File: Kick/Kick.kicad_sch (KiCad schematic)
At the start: 8 parts, among them J1 CN1 / J11, J2 CN2 / J12, U0 NOIP1SN1300A-QTI, U1 NOIP1SN1300A-QTI, U2 NX3L4053, U3 NX3L4053

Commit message: started PCB routing with new voltage regulators
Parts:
- added C1, C2: C, Capacitor_SMD:C_0603_1608Metric, symbol Device:C
- added U4: MIC5504-1.8YM5, Package_TO_SOT_SMD:SOT-23-5, symbol Regulator_Linear:MIC5504-1.8YM5
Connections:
- net +1V8: now also C2.1, U4.5 (VOUT); no longer J1.5 (Pin_5)
- net +3.3V: now also U4.3 (EN)
- net +3V3: now also C1.1, U4.1 (VIN)
- net GND: now also C1.2, C2.2, U4.2 (GND)
- no-connect marks 101 -> 102

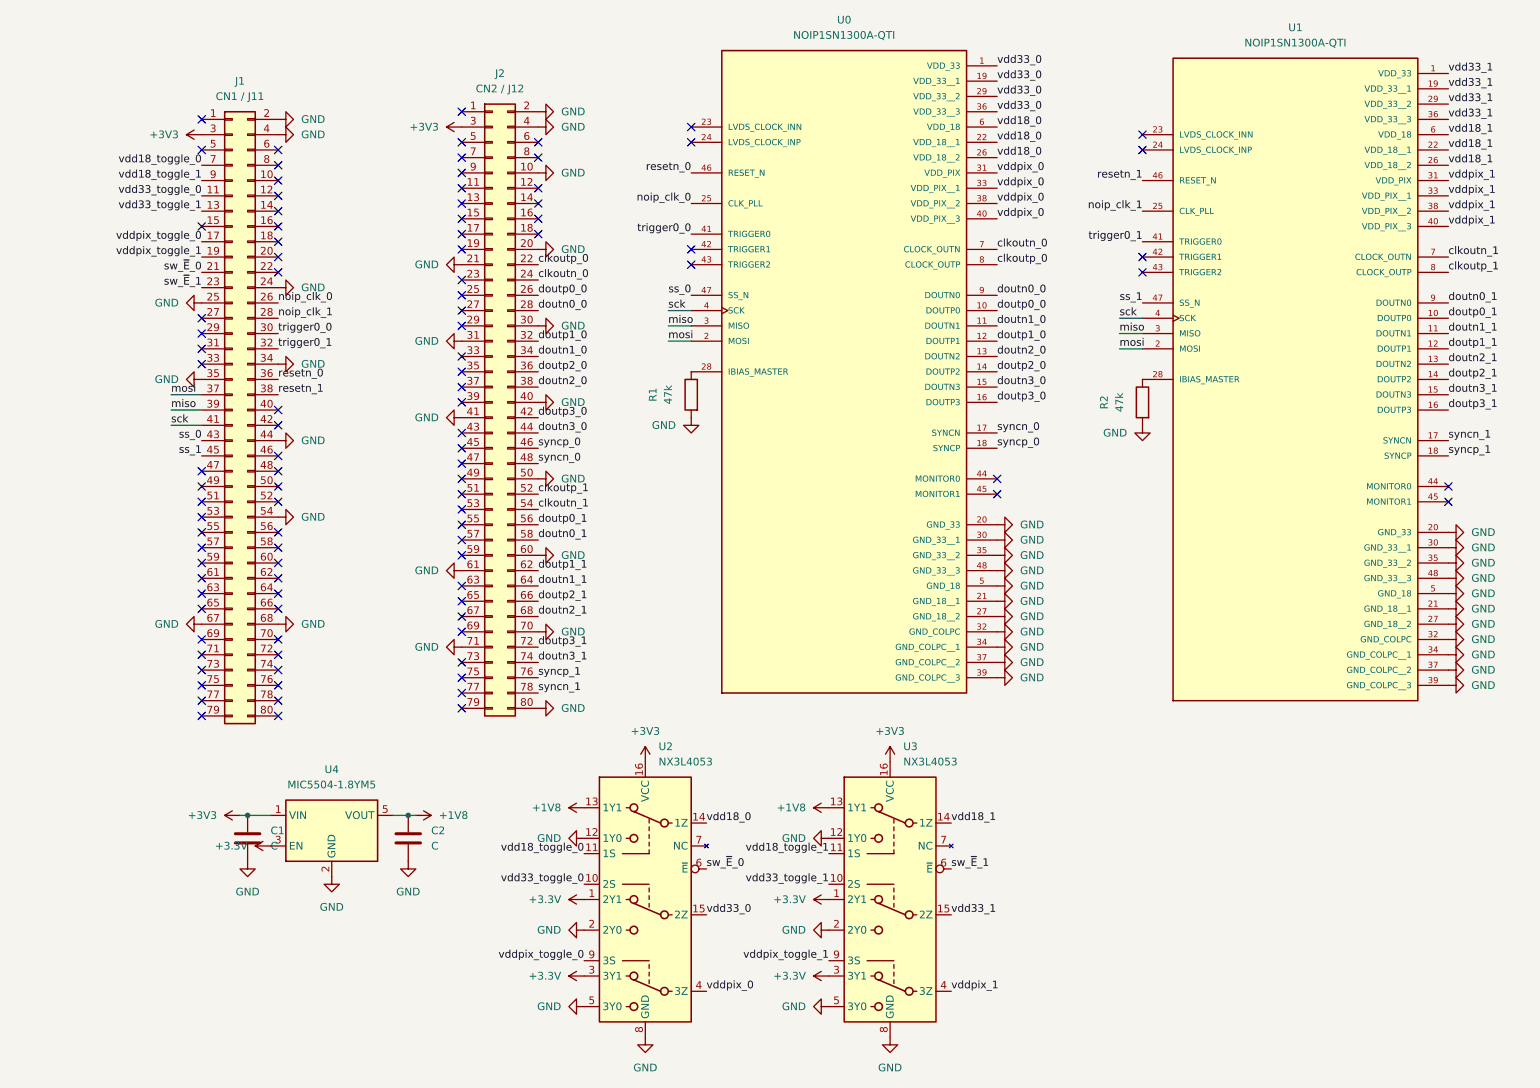
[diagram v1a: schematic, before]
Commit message: acurrate placement of devices, HF impedance calculation
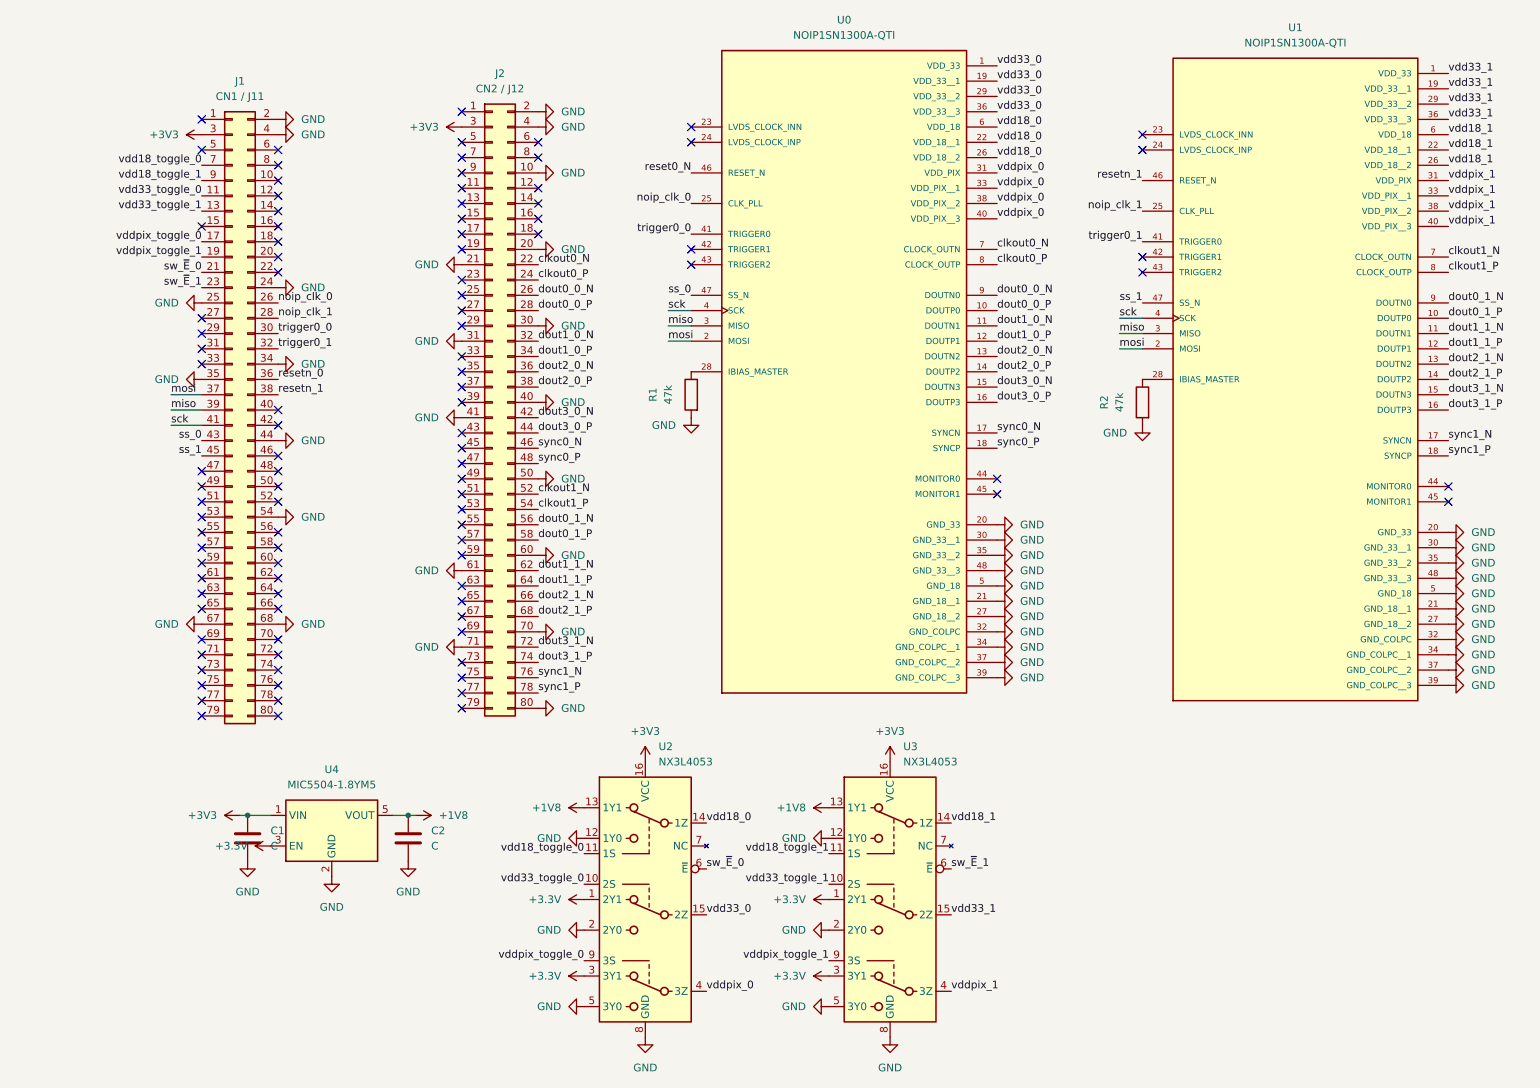
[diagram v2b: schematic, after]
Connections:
- net resetn_0: no longer U0.46 (RESET_N)
- net clkoutn_0 renamed clkout0_N
- net clkout0_N: now also J2.22 (Pin_22); no longer J2.24 (Pin_24)
- net clkoutn_1 renamed clkout1_N
- net clkout1_N: now also J2.52 (Pin_52); no longer J2.54 (Pin_54)
- net clkoutp_0 renamed clkout0_P
- net clkout0_P: now also J2.24 (Pin_24); no longer J2.22 (Pin_22)
- net clkoutp_1 renamed clkout1_P
- net clkout1_P: now also J2.54 (Pin_54); no longer J2.52 (Pin_52)
- net doutn0_0 renamed dout0_0_N
- net dout0_0_N: now also J2.26 (Pin_26); no longer J2.28 (Pin_28)
- net doutn0_1 renamed dout0_1_N
- net dout0_1_N: now also J2.56 (Pin_56); no longer J2.58 (Pin_58)
- net doutn1_0 renamed dout1_0_N
- net dout1_0_N: now also J2.32 (Pin_32); no longer J2.34 (Pin_34)
- net doutn1_1 renamed dout1_1_N
- net dout1_1_N: now also J2.62 (Pin_62); no longer J2.64 (Pin_64)
- net doutn2_0 renamed dout2_0_N
- net dout2_0_N: now also J2.36 (Pin_36); no longer J2.38 (Pin_38)
- net doutn2_1 renamed dout2_1_N
- net dout2_1_N: now also J2.66 (Pin_66); no longer J2.68 (Pin_68)
- net doutn3_0 renamed dout3_0_N
- net dout3_0_N: now also J2.42 (Pin_42); no longer J2.44 (Pin_44)
- net doutn3_1 renamed dout3_1_N
- net dout3_1_N: now also J2.72 (Pin_72); no longer J2.74 (Pin_74)
- net doutp0_0 renamed dout0_0_P
- net dout0_0_P: now also J2.28 (Pin_28); no longer J2.26 (Pin_26)
- net doutp0_1 renamed dout0_1_P
- net dout0_1_P: now also J2.58 (Pin_58); no longer J2.56 (Pin_56)
- net doutp1_0 renamed dout1_0_P
- net dout1_0_P: now also J2.34 (Pin_34); no longer J2.32 (Pin_32)
- net doutp1_1 renamed dout1_1_P
- net dout1_1_P: now also J2.64 (Pin_64); no longer J2.62 (Pin_62)
- net doutp2_0 renamed dout2_0_P
- net dout2_0_P: now also J2.38 (Pin_38); no longer J2.36 (Pin_36)
- net doutp2_1 renamed dout2_1_P
- net dout2_1_P: now also J2.68 (Pin_68); no longer J2.66 (Pin_66)
- net doutp3_0 renamed dout3_0_P
- net dout3_0_P: now also J2.44 (Pin_44); no longer J2.42 (Pin_42)
- net doutp3_1 renamed dout3_1_P
- net dout3_1_P: now also J2.74 (Pin_74); no longer J2.72 (Pin_72)
- net syncn_0 renamed sync0_N
- net sync0_N: now also J2.46 (Pin_46); no longer J2.48 (Pin_48)
- net syncn_1 renamed sync1_N
- net sync1_N: now also J2.76 (Pin_76); no longer J2.78 (Pin_78)
- net syncp_0 renamed sync0_P
- net sync0_P: now also J2.48 (Pin_48); no longer J2.46 (Pin_46)
- net syncp_1 renamed sync1_P
- net sync1_P: now also J2.78 (Pin_78); no longer J2.76 (Pin_76)
- new net reset0_N: U0.46 (RESET_N)
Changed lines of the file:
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@@
 		)
 	)
-	(label "doutp0_1"
-		(at 100.33 105.41 0)
+	(label "dout0_1_P"
+		(at 100.33 107.95 0)
 		(fields_autoplaced yes)
 		(effects
@@
 		)
 	)
-	(label "syncp_0"
-		(at 100.33 92.71 0)
+	(label "sync0_P"
+		(at 100.33 95.25 0)
 		(fields_autoplaced yes)
 		(effects
@@
 		)
 	)
-	(label "syncn_1"
-		(at 100.33 133.35 0)
+	(label "sync1_N"
+		(at 100.33 130.81 0)
 		(fields_autoplaced yes)
 		(effects
@@
 		)
 	)
-	(label "doutn1_1"
+	(label "dout1_1_N"
 		(at 251.46 73.66 0)
 		(fields_autoplaced yes)
@@
 		)
 	)
-	(label "clkoutp_0"
-		(at 100.33 62.23 0)
+	(label "clkout0_P"
+		(at 100.33 64.77 0)
 		(fields_autoplaced yes)
 		(effects
@@
 		)
 	)
-	(label "clkoutn_1"
-		(at 100.33 102.87 0)
+	(label "clkout1_N"
+		(at 100.33 100.33 0)
 		(fields_autoplaced yes)
 		(effects
@@
 		)
 	)
-	(label "doutp1_1"
+	(label "dout1_1_P"
 		(at 251.46 76.2 0)
 		(fields_autoplaced yes)
@@
 		)
 	)
-	(label "doutn2_1"
+	(label "dout2_1_N"
 		(at 251.46 78.74 0)
 		(fields_autoplaced yes)
@@
 		)
 	)
-	(label "syncn_0"
+	(label "sync0_N"
 		(at 176.53 90.17 0)
 		(fields_autoplaced yes)
@@
 		)
 	)
-	(label "doutp1_0"
+	(label "dout1_0_P"
 		(at 176.53 74.93 0)
 		(fields_autoplaced yes)
@@
 		)
 	)
-	(label "doutn0_1"
+	(label "dout0_1_N"
 		(at 251.46 68.58 0)
 		(fields_autoplaced yes)
@@
 		)
 	)
-	(label "syncn_0"
-		(at 100.33 95.25 0)
+	(label "sync0_N"
+		(at 100.33 92.71 0)
 		(fields_autoplaced yes)
 		(effects
@@
 		)
 	)
-	(label "doutp3_1"
-		(at 100.33 125.73 0)
+	(label "dout3_1_P"
+		(at 100.33 128.27 0)
 		(fields_autoplaced yes)
 		(effects
@@
 		)
 	)
-	(label "doutp2_1"
-		(at 100.33 118.11 0)
+	(label "dout2_1_P"
+		(at 100.33 120.65 0)
 		(fields_autoplaced yes)
 		(effects
@@
 		)
 	)
-	(label "doutn3_1"
+	(label "dout3_1_N"
 		(at 251.46 83.82 0)
 		(fields_autoplaced yes)
@@
 		)
 	)
-	(label "doutn0_0"
-		(at 100.33 69.85 0)
+	(label "dout0_0_N"
+		(at 100.33 67.31 0)
 		(fields_autoplaced yes)
 		(effects
@@
 		)
 	)
-	(label "syncn_1"
+	(label "sync1_N"
 		(at 251.46 91.44 0)
 		(fields_autoplaced yes)
@@
 		)
 	)
-	(label "doutp2_1"
+	(label "dout2_1_P"
 		(at 251.46 81.28 0)
 		(fields_autoplaced yes)
@@
 		)
 	)
-	(label "doutn0_1"
-		(at 100.33 107.95 0)
+	(label "dout0_1_N"
+		(at 100.33 105.41 0)
 		(fields_autoplaced yes)
 		(effects
@@
 		)
 	)
-	(label "clkoutp_1"
-		(at 100.33 100.33 0)
+	(label "clkout1_P"
+		(at 100.33 102.87 0)
 		(fields_autoplaced yes)
 		(effects
@@
 		)
 	)
-	(label "doutn1_0"
-		(at 100.33 77.47 0)
+	(label "dout1_0_N"
+		(at 100.33 74.93 0)
 		(fields_autoplaced yes)
 		(effects
@@
 		)
 	)
-	(label "doutp3_0"
-		(at 100.33 87.63 0)
+	(label "dout3_0_P"
+		(at 100.33 90.17 0)
 		(fields_autoplaced yes)
 		(effects
@@
 		)
 	)
-	(label "clkoutn_0"
+	(label "clkout0_N"
 		(at 176.53 59.69 0)
 		(fields_autoplaced yes)
@@
 		)
 	)
-	(label "clkoutp_0"
+	(label "clkout0_P"
 		(at 176.53 62.23 0)
 		(fields_autoplaced yes)
@@
 		)
 	)
-	(label "doutn2_1"
-		(at 100.33 120.65 0)
+	(label "dout2_1_N"
+		(at 100.33 118.11 0)
 		(fields_autoplaced yes)
 		(effects
@@
 		)
 	)
-	(label "doutp0_0"
+	(label "dout0_0_P"
 		(at 176.53 69.85 0)
 		(fields_autoplaced yes)
@@
 		)
 	)
-	(label "doutn3_0"
-		(at 100.33 90.17 0)
+	(label "dout3_0_N"
+		(at 100.33 87.63 0)
 		(fields_autoplaced yes)
 		(effects
@@
 		)
 	)
-	(label "doutn3_0"
+	(label "dout3_0_N"
 		(at 176.53 82.55 0)
 		(fields_autoplaced yes)
@@
 		)
 	)
-	(label "doutp1_0"
-		(at 100.33 74.93 0)
+	(label "dout1_0_P"
+		(at 100.33 77.47 0)
 		(fields_autoplaced yes)
 		(effects
@@
 		)
 	)
-	(label "doutn1_1"
-		(at 100.33 115.57 0)
+	(label "dout1_1_N"
+		(at 100.33 113.03 0)
 		(fields_autoplaced yes)
 		(effects
@@
 		)
 	)
-	(label "syncp_0"
+	(label "sync0_P"
 		(at 176.53 92.71 0)
 		(fields_autoplaced yes)
@@
 		)
 	)
-	(label "doutn3_1"
-		(at 100.33 128.27 0)
+	(label "dout3_1_N"
+		(at 100.33 125.73 0)
 		(fields_autoplaced yes)
 		(effects
@@
 		)
 	)
-	(label "doutp0_0"
-		(at 100.33 67.31 0)
+	(label "dout0_0_P"
+		(at 100.33 69.85 0)
 		(fields_autoplaced yes)
 		(effects
@@
 		)
 	)
-	(label "syncp_1"
-		(at 100.33 130.81 0)
+	(label "sync1_P"
+		(at 100.33 133.35 0)
 		(fields_autoplaced yes)
 		(effects
@@
 		)
 	)
-	(label "doutn1_0"
+	(label "dout1_0_N"
 		(at 176.53 72.39 0)
 		(fields_autoplaced yes)
@@
 		)
 	)
-	(label "doutp3_1"
+	(label "dout3_1_P"
 		(at 251.46 86.36 0)
 		(fields_autoplaced yes)
@@
 		)
 	)
-	(label "syncp_1"
+	(label "sync1_P"
 		(at 251.46 93.98 0)
 		(fields_autoplaced yes)
@@
 		)
 	)
-	(label "doutn2_0"
+	(label "dout2_0_N"
 		(at 176.53 77.47 0)
 		(fields_autoplaced yes)
@@
 		)
 	)
-	(label "doutp2_0"
-		(at 100.33 80.01 0)
+	(label "dout2_0_P"
+		(at 100.33 82.55 0)
 		(fields_autoplaced yes)
 		(effects
@@
 		)
 	)
-	(label "doutp2_0"
+	(label "dout2_0_P"
 		(at 176.53 80.01 0)
 		(fields_autoplaced yes)
@@
 		)
 	)
-	(label "resetn_0"
+	(label "reset0_N"
 		(at 125.73 46.99 180)
 		(fields_autoplaced yes)
@@
 		)
 	)
-	(label "doutp1_1"
-		(at 100.33 113.03 0)
+	(label "dout1_1_P"
+		(at 100.33 115.57 0)
 		(fields_autoplaced yes)
 		(effects
@@
 		)
 	)
-	(label "doutp3_0"
+	(label "dout3_0_P"
 		(at 176.53 85.09 0)
 		(fields_autoplaced yes)
@@
 		)
 	)
-	(label "doutn0_0"
+	(label "dout0_0_N"
 		(at 176.53 67.31 0)
 		(fields_autoplaced yes)
@@
 		)
 	)
-	(label "clkoutn_0"
-		(at 100.33 64.77 0)
+	(label "clkout0_N"
+		(at 100.33 62.23 0)
 		(fields_autoplaced yes)
 		(effects
@@
 		)
 	)
-	(label "doutp0_1"
+	(label "dout0_1_P"
 		(at 251.46 71.12 0)
 		(fields_autoplaced yes)
@@
 		)
 	)
-	(label "doutn2_0"
-		(at 100.33 82.55 0)
+	(label "dout2_0_N"
+		(at 100.33 80.01 0)
 		(fields_autoplaced yes)
 		(effects
@@
 		)
 	)
-	(label "clkoutn_1"
+	(label "clkout1_N"
 		(at 251.46 60.96 0)
 		(fields_autoplaced yes)
@@
 		)
 	)
-	(label "clkoutp_1"
+	(label "clkout1_P"
 		(at 251.46 63.5 0)
 		(fields_autoplaced yes)
@@
 	)
 	(symbol
-		(lib_name "NX3L4053:NX3L4053")
 		(lib_id "NX3L4053:NX3L4053")
 		(at 158.75 162.56 0)
@@
 	)
 	(symbol
-		(lib_name "NX3L4053:NX3L4053")
 		(lib_id "NX3L4053:NX3L4053")
 		(at 118.11 162.56 0)

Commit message: optimized placement of via next to the 2 NOIP2
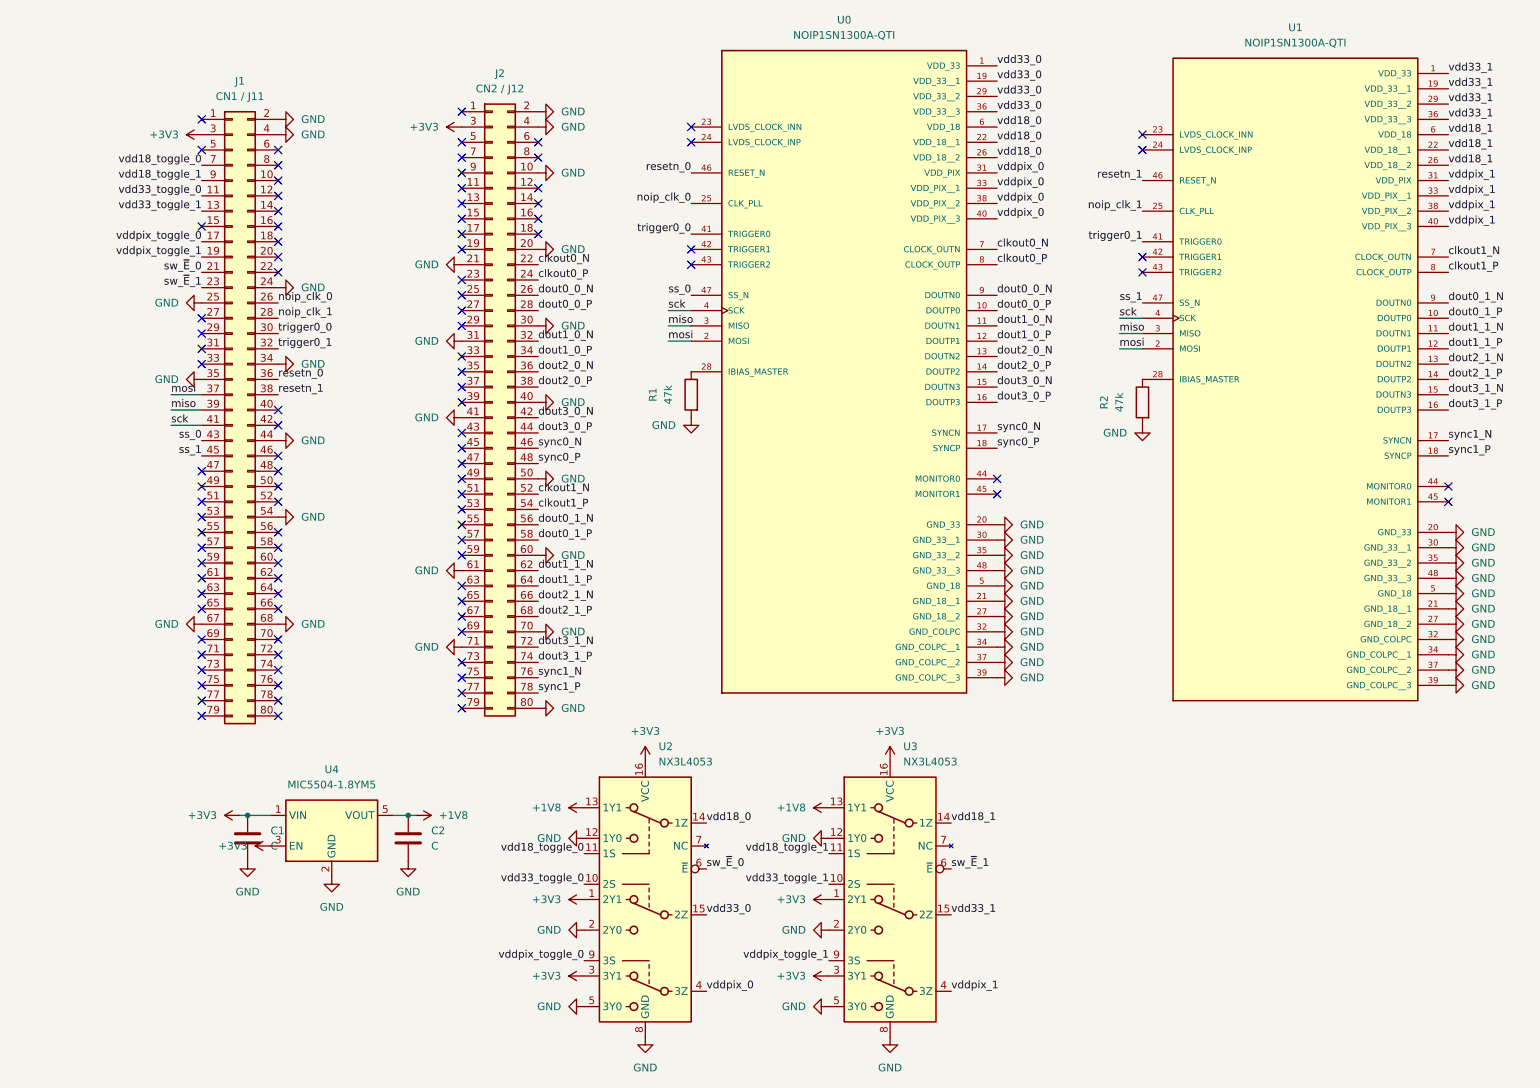
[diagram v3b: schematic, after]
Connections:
- net +3.3V is gone; now on net +3V3: U2.1 (2Y1), U2.3 (3Y1), U3.1 (2Y1), U3.3 (3Y1), U4.3 (EN)
- net reset0_N is gone; now on net resetn_0: U0.46 (RESET_N)
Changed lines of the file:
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@@
 		)
 	)
-	(label "reset0_N"
+	(label "resetn_0"
 		(at 125.73 46.99 180)
 		(fields_autoplaced yes)
@@
 			)
 		)
-		(property "Value" "+3.3V"
+		(property "Value" "+3V3"
 			(at 52.07 158.7499 90)
 			(effects
@@
 			)
 		)
-		(property "Value" "+3.3V"
+		(property "Value" "+3V3"
 			(at 144.78 167.6401 90)
 			(effects
@@
 			)
 		)
-		(property "Value" "+3.3V"
+		(property "Value" "+3V3"
 			(at 104.14 180.3401 90)
 			(effects
@@
 			)
 		)
-		(property "Value" "+3.3V"
+		(property "Value" "+3V3"
 			(at 144.78 180.3401 90)
 			(effects
@@
 			)
 		)
-		(property "Value" "+3.3V"
+		(property "Value" "+3V3"
 			(at 104.14 167.6401 90)
 			(effects
